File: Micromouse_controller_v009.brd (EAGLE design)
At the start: 50.8 x 43.2 mm, 17 parts, among them IC2 TA4805BF, U1 ATMEGA328P_TQFP

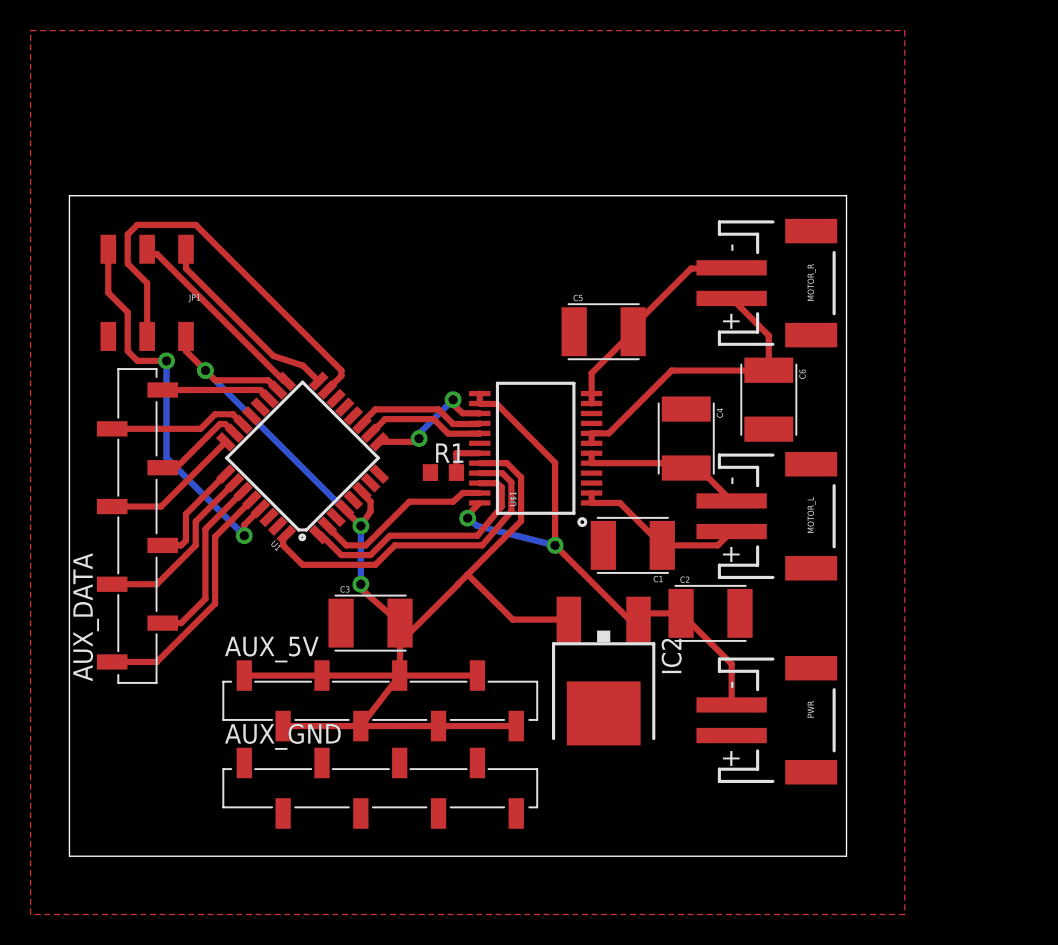
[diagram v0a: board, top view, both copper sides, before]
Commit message: Version 1.0 of Micromouse controller 	Added capacitor values 	Arranged Labels 	Completed BoM and Presentation
Signed-off-by: Matthew Lumantas <mluma001@ucr.edu>
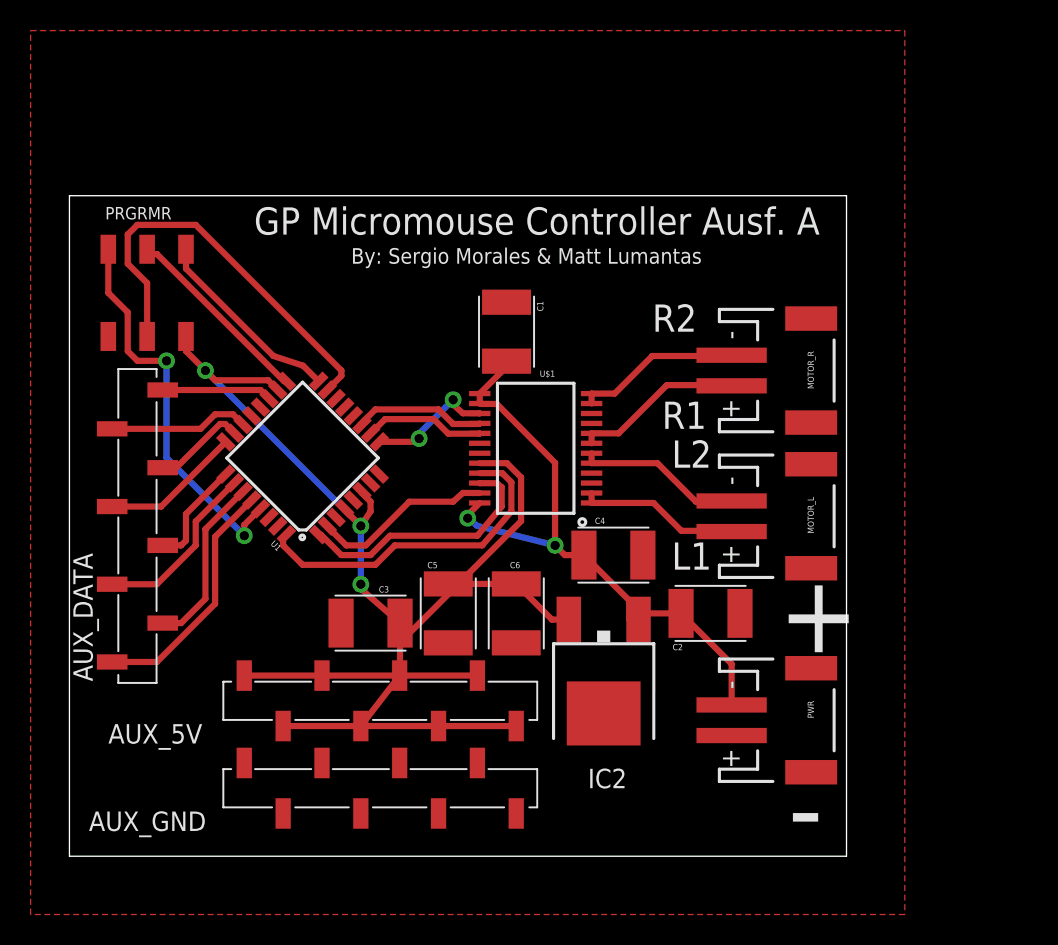
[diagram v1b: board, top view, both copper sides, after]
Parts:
- removed R1: 10k, resistor:R0603
- C1, C6: value (none) -> 10uF
- C2, C3: value (none) -> 1uF
- C4, C5: value (none) -> 0.1uF
- moved C6 21.6 mm to (29.2, 15.9)
- moved C5 21.0 mm to (24.8, 15.9), turned to 270 degrees
- moved C1 16.2 mm to (28.6, 34.3), turned to 270 degrees
- moved C4 8.99 mm to (35.6, 19.7), turned to 180 degrees
- moved MOTOR_R 5.72 mm to (47.0, 31.8)
- renumbered JP1 to PRGRMR
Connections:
- net +12V: now also C1.A, C4.A
- net +5V: now also C5.C, C6.C
- net GND: now also C1.C, C5.A; no longer C1.A, C5.C, R1.1
- net N$11: no longer C1.C
- net N$12: no longer C4.A
- net N$13: no longer C5.A
- net N$14: no longer C6.C
- net STBY: no longer R1.2
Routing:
- net N$14: track 19.6 -> 11.1 mm
- net +12V: track 37.7 -> 41.3 mm
- net N$13: track 14.2 -> 10.8 mm
- net STBY: track 2.80 -> 0.00 mm
- net +5V: track 97.2 -> 98.5 mm
- net N$11: track 11.3 -> 10.6 mm
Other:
- board text added: "+"
- board text added: "-"
- board text added: "By: Sergio Morales & Matt Lumantas"
- board text added: "GP Micromouse Controller Ausf. A"
- board text added: "L1"
- board text added: "L2"
- board text added: "R1"
- board text added: "R2"
